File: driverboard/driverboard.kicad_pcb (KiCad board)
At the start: 2 copper layers, 57.7 x 55.4 mm, 30 parts, among them IC1 NCV7240ADPR2G, J1 valve 1, J10 data output, J11 12V input, J12 12V output, J2 valve 2, J3 valve 3, J4 valve 4, J5 valve 5, J6 valve 6, J7 valve 7, J8 valve 8, J9 data input, U1 74LVC1G34

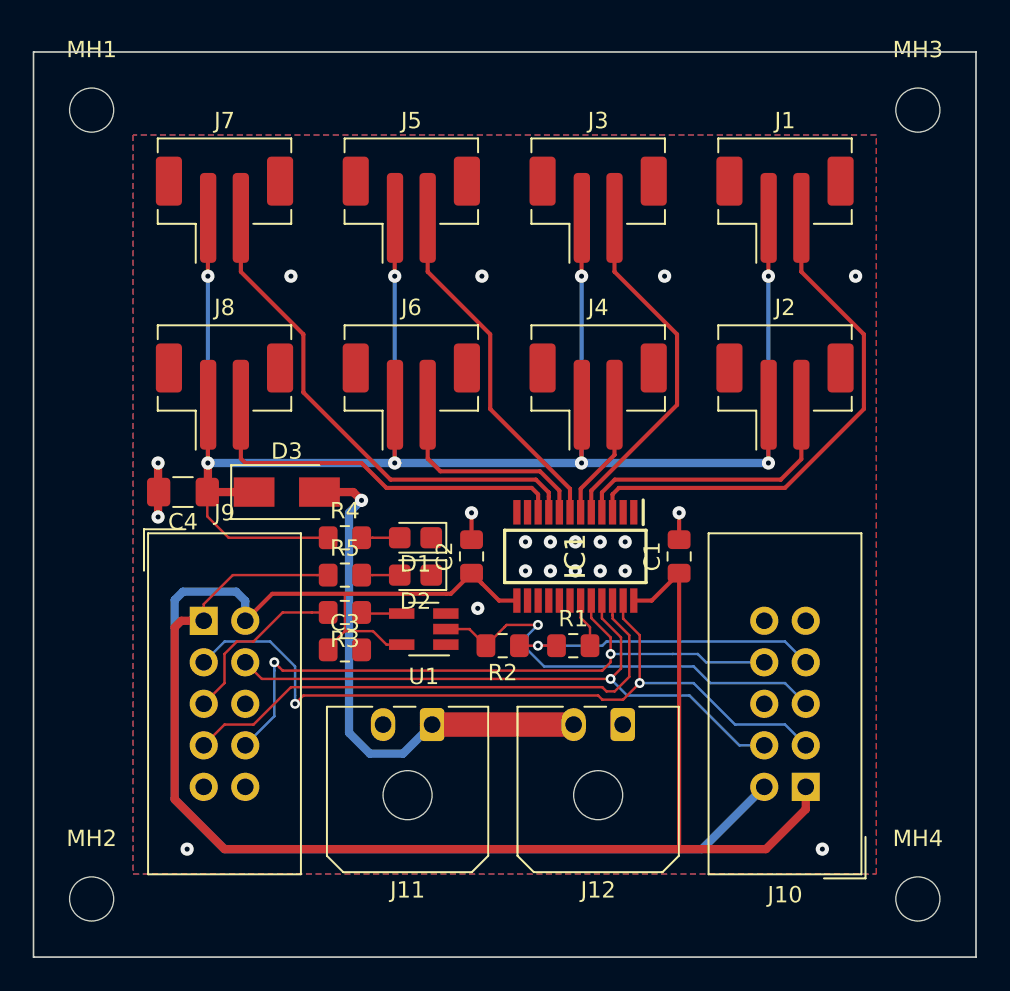
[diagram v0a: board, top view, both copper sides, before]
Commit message: add labels
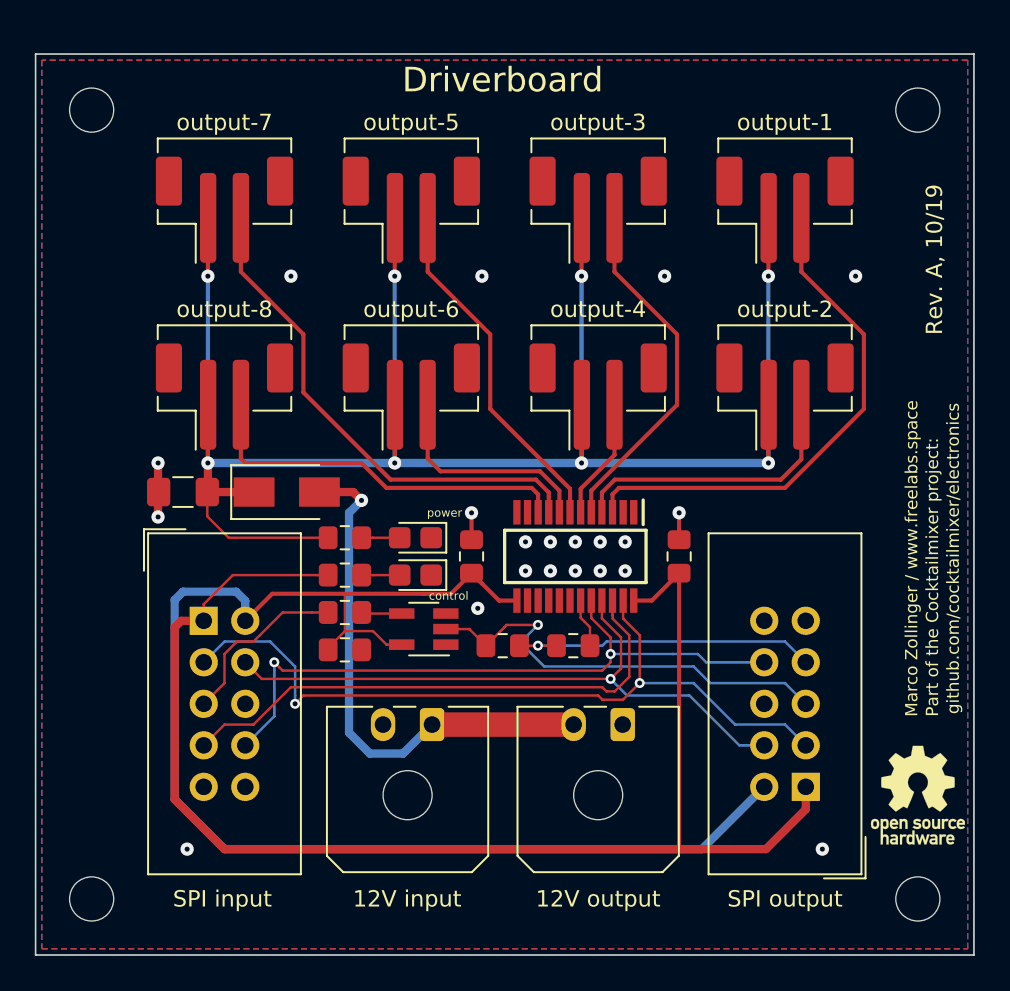
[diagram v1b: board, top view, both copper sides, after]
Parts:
- added REF**: OSHW-Logo_5.7x6mm_SilkScreen, Symbol:OSHW-Logo_5.7x6mm_SilkScreen, F.Cu at (98.3, 179.1)
- D1: value yellow -> power
- D2: value green -> control
- J1: value valve 1 -> output-1
- J10: value data output -> SPI output
- J2: value valve 2 -> output-2
- J3: value valve 3 -> output-3
- J4: value valve 4 -> output-4
- J5: value valve 5 -> output-5
- J6: value valve 6 -> output-6
- J7: value valve 7 -> output-7
- J8: value valve 8 -> output-8
- J9: value data input -> SPI input
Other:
- board size 57.7 x 55.4 mm -> 57.4 x 55.1 mm
- board text added: "Driverboard"
- board text added: "Marco Zollinger / www.freelabs.space"
- board text added: "Part of the Cocktailmixer project:"
- board text added: "Rev. A, 10/19"
- board text added: "github.com/cocktailmixer/electronics"
